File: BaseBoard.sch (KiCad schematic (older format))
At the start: 128 parts, among them U1 TLC5971PWP, U10 TLC5971PWP, U11 TLC5971PWP, U12 TLC5971PWP, U13 TLC5971PWP, U14 TLC5971PWP, U15 TLC5971PWP, U16 TLC5971PWP, U2 TLC5971PWP, U3 TLC5971PWP, U4 TLC5971PWP, U5 TLC5971PWP, U6 TLC5971PWP, U7 TLC5971PWP, U8 TLC5971PWP, U9 TLC5971PWP

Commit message: Reworked schematics
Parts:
- removed C1, C10, C11, C12, C13, C14, C15, C16, C17, C18, C19, C2, C20, C21, C22, C23, C24, C25, C26, C27, C28, C29, C3, C30, C31, C32, C4, C5, C6, C7, C8, C9: 1uF, symbol Device:C
- removed R1, R10, R11, R12, R13, R14, R15, R16, R2, R3, R4, R5, R6, R7, R8, R9: 1K, symbol Device:R
- removed U1, U10, U11, U12, U13, U14, U15, U16, U2, U3, U4, U5, U6, U7, U8, U9: TLC5971PWP, Package_SO:HTSSOP-20-1EP_4.4x6.5mm_P0.65mm_EP3.4x6.5mm_Mask2.75x3.43mm_ThermalVias, symbol Driver_LED:TLC5971PWP
- added ANOD1: Anodes, symbol BaseBoard:Anodes
- added C? (x32): 1uF, symbol Device:C
- added CNTL1: ESP32_NodeMCU, symbol BaseBoard:ESP32_NodeMCU
- added Q? (x8): IRLML6401TRPBF, digikey-footprints:SOT-23-3, symbol dk_Transistors-FETs-MOSFETs-Single:IRLML6401TRPBF
- added Q? (x8): MMBT2222A-7-F, digikey-footprints:SOT-23-3, symbol dk_Transistors-Bipolar-BJT-Single:MMBT2222A-7-F
- added R? (x32): 1K, symbol Device:R
- added R? (x8): 10, symbol Device:R
- added U1, U10, U11, U12, U13, U14, U15, U16, U2, U3, U4, U5, U6, U7, U8, U9: TLC59711PWPR, digikey-footprints:TSSOP-20-1EP_W4.4mm, symbol BaseBoard:TLC59711PWPR_Reordered
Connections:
- net labels added: VCC
- net labels removed: +5V
- wire segments 326 -> 463
- no-connect marks 0 -> 2

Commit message: Add anotations
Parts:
- removed C? (x32): 1uF, symbol Device:C
- removed R? (x16): 1K, symbol Device:R
- added C1, C10, C11, C12, C13, C14, C15, C16, C17, C18, C19, C2, C20, C21, C22, C23, C24, C25, C26, C27, C28, C29, C3, C30, C31, C32, C4, C5, C6, C7, C8, C9: 1uF, symbol Device:C
- added R25, R26, R27, R28, R29, R30, R31, R32, R33, R34, R35, R36, R37, R38, R39, R40: 1K, symbol Device:R
- gave numbers to parts that had none: 40

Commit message: Add footprints to common components
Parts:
- C1, C10, C11, C12, C13, C14, C15, C16, C17, C18, C19, C2, C20, C21, C22, C23, C24, C25, C26, C27, C28, C29, C3, C30, C31, C32, C4, C5, C6, C7, C8, C9: footprint (none) -> Capacitor_SMD:C_0805_2012Metric_Pad1.15x1.40mm_HandSolder
- CNTL1: footprint (none) -> BaseBoard:ESP32_NodeMCU
- R1, R10, R11, R12, R13, R14, R15, R16, R17, R18, R19, R2, R20, R21, R22, R23, R24, R25, R26, R27, R28, R29, R3, R30, R31, R32, R33, R34, R35, R36, R37, R38, R39, R4, R40, R5, R6, R7, R8, R9: footprint (none) -> Resistor_SMD:R_0805_2012Metric_Pad1.15x1.40mm_HandSolder

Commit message: Fix lots of fuckups
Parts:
- removed Q1, Q11, Q13, Q3, Q5, Q7, Q9: IRLML6401TRPBF, digikey-footprints:SOT-23-3, symbol dk_Transistors-FETs-MOSFETs-Single:IRLML6401TRPBF
- removed Q10, Q12, Q14, Q2, Q4, Q6, Q8: MMBT2222A-7-F, digikey-footprints:SOT-23-3, symbol dk_Transistors-Bipolar-BJT-Single:MMBT2222A-7-F
- removed U1, U10, U11, U12, U13, U14, U15, U16, U2, U3, U4, U5, U6, U7, U8, U9: TLC59711PWPR, digikey-footprints:TSSOP-20-1EP_W4.4mm, symbol BaseBoard:TLC59711PWPR_Reordered
- added Q1, Q11, Q13, Q3, Q5, Q7, Q9: MMBT2222A-7-F, digikey-footprints:SOT-23-3, symbol dk_Transistors-Bipolar-BJT-Single:MMBT2222A-7-F
- added Q10, Q12, Q14, Q2, Q4, Q6, Q8: IRLML6401TRPBF, digikey-footprints:SOT-23-3, symbol dk_Transistors-FETs-MOSFETs-Single:IRLML6401TRPBF
- added U1, U10, U11, U12, U13, U14, U15, U16, U2, U3, U4, U5, U6, U7, U8, U9: TLC5971PWPR, digikey-footprints:TSSOP-20-1EP_W4.4mm, symbol BaseBoard:TLC5971PWPR_Reordered
- R1, R10, R13, R16, R19, R22, R4, R7: footprint Resistor_SMD:R_0805_2012Metric_Pad1.15x1.40mm_HandSolder -> (none)
- R11, R14, R17, R2, R20, R23, R5, R8: value 10 -> 1K; footprint Resistor_SMD:R_0805_2012Metric_Pad1.15x1.40mm_HandSolder -> (none)
- R12, R15, R18, R21, R24, R3, R6, R9: value 1K -> 10; footprint Resistor_SMD:R_0805_2012Metric_Pad1.15x1.40mm_HandSolder -> (none)
- R25, R26, R27, R28, R29, R30, R31, R32, R33, R34, R35, R36, R37, R38, R39, R40: value 1K -> 3.3K
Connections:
- wire segments 463 -> 470
- no-connect marks 2 -> 28
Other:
- moved on the sheet: ANOD1, Q15, Q16

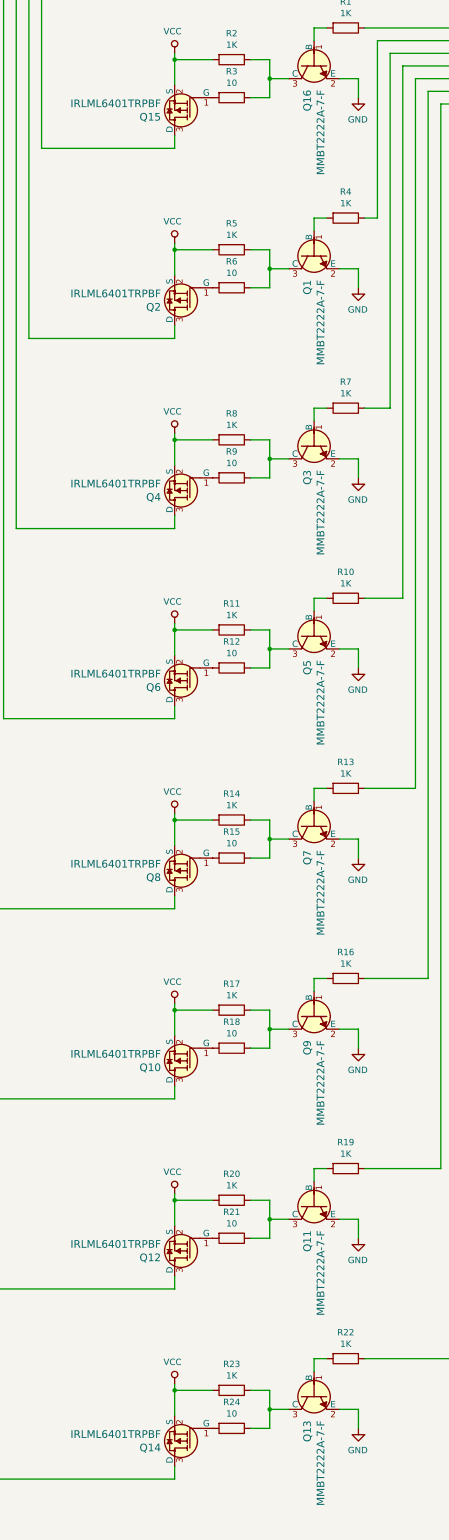
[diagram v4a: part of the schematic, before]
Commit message: Add PCB base
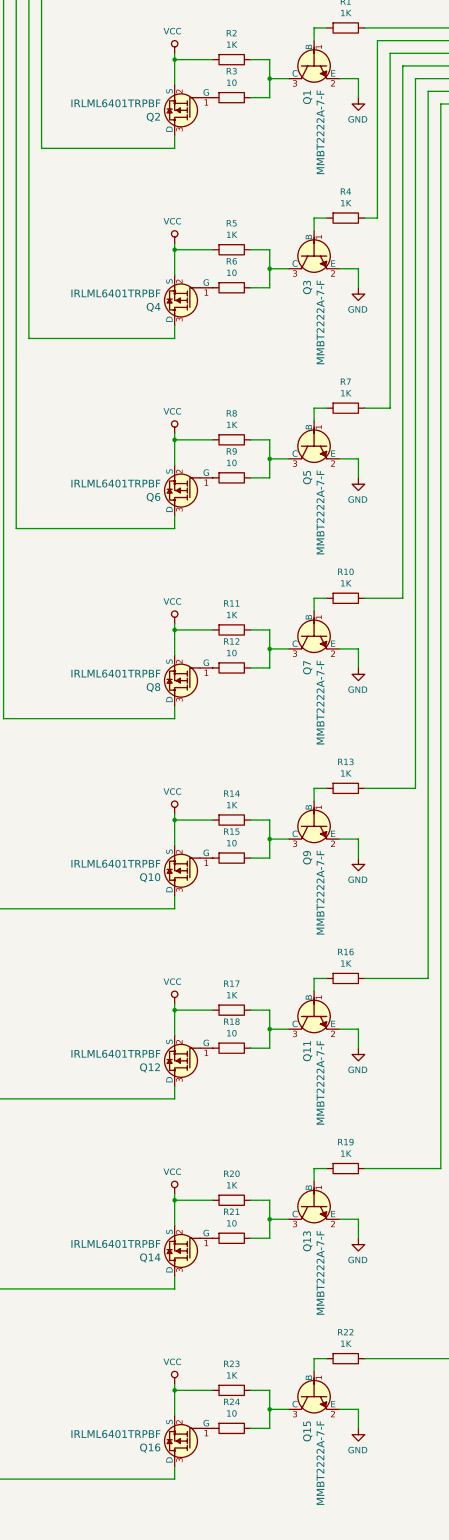
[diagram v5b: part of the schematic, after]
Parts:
- ANOD1: footprint (none) -> BaseBoard:Anodes
- R1, R10, R11, R12, R13, R14, R15, R16, R17, R18, R19, R2, R20, R21, R22, R23, R24, R3, R4, R5, R6, R7, R8, R9: footprint (none) -> Resistor_SMD:R_0805_2012Metric_Pad1.15x1.40mm_HandSolder
- renumbered Q16 to Q15, Q15 to Q16
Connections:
- net at R2.1, R3.1: now also Q1.3 (C); no longer Q15.3 (C)
- net at R3.2: now also Q2.1 (G); no longer Q16.1 (G)
- net at Q16.3 (D): now also ANOD1.8 (A8); no longer ANOD1.1 (A1)
- net at Q15.1 (B): now also R22.2; no longer R1.2
- net at Q1.1 (B): now also R1.2; no longer R4.2
- net at R5.1, R6.1: now also Q3.3 (C); no longer Q1.3 (C)
- net at R6.2: now also Q4.1 (G); no longer Q2.1 (G)
- net at Q2.3 (D): now also ANOD1.1 (A1); no longer ANOD1.2 (A2)
- net at Q3.1 (B): now also R4.2; no longer R7.2
- net at R8.1, R9.1: now also Q5.3 (C); no longer Q3.3 (C)
- net at R9.2: now also Q6.1 (G); no longer Q4.1 (G)
- net at Q4.3 (D): now also ANOD1.2 (A2); no longer ANOD1.3 (A3)
- net at Q5.1 (B): now also R7.2; no longer R10.2
- net at R11.1, R12.1: now also Q7.3 (C); no longer Q5.3 (C)
- net at R12.2: now also Q8.1 (G); no longer Q6.1 (G)
- net at Q6.3 (D): now also ANOD1.3 (A3); no longer ANOD1.4 (A4)
- net at Q7.1 (B): now also R10.2; no longer R13.2
- net at R14.1, R15.1: now also Q9.3 (C); no longer Q7.3 (C)
- net at R15.2: now also Q10.1 (G); no longer Q8.1 (G)
- net at Q8.3 (D): now also ANOD1.4 (A4); no longer ANOD1.5 (A5)
- net at Q9.1 (B): now also R13.2; no longer R16.2
- net at R17.1, R18.1: now also Q11.3 (C); no longer Q9.3 (C)
- net at R18.2: now also Q12.1 (G); no longer Q10.1 (G)
- net at Q10.3 (D): now also ANOD1.5 (A5); no longer ANOD1.6 (A6)
- net at Q11.1 (B): now also R16.2; no longer R19.2
- net at R20.1, R21.1: now also Q13.3 (C); no longer Q11.3 (C)
- net at R21.2: now also Q14.1 (G); no longer Q12.1 (G)
- net at Q12.3 (D): now also ANOD1.6 (A6); no longer ANOD1.7 (A7)
- net at Q13.1 (B): now also R19.2; no longer R22.2
- net at R23.1, R24.1: now also Q15.3 (C); no longer Q13.3 (C)
- net at R24.2: now also Q16.1 (G); no longer Q14.1 (G)
- net at Q14.3 (D): now also ANOD1.7 (A7); no longer ANOD1.8 (A8)
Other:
- moved on the sheet: Q1, Q10, Q11, Q12, Q13, Q14, Q15, Q16, Q2, Q3, Q4, Q5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

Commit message: Update footprints
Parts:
- U1, U10, U11, U12, U13, U14, U15, U16, U2, U3, U4, U5, U6, U7, U8, U9: footprint digikey-footprints:TSSOP-20-1EP_W4.4mm -> Package_SO:HTSSOP-20-1EP_4.4x6.5mm_P0.65mm_EP3.4x6.5mm_Mask2.75x3.43mm_ThermalVias
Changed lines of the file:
@@
 F 0 "U4" H 18150 3453 60  0000 C CNN
 F 1 "TLC5971PWPR" H 18150 3347 60  0000 C CNN
-F 2 "digikey-footprints:TSSOP-20-1EP_W4.4mm" H 18300 2950 60  0001 L CNN
+F 2 "Package_SO:HTSSOP-20-1EP_4.4x6.5mm_P0.65mm_EP3.4x6.5mm_Mask2.75x3.43mm_ThermalVias" H 18300 2950 60  0001 L CNN
 F 3 "http://www.ti.com/general/docs/suppproductinfo.tsp?distId=10&gotoUrl=http%3A%2F%2Fwww.ti.com%2Flit%2Fgpn%2Ftlc5971" H 18300 3050 60  0001 L CNN
 F 4 "296-27796-1-ND" H 18300 3150 60  0001 L CNN "Digi-Key_PN"
@@
 F 0 "U3" H 15900 3453 60  0000 C CNN
 F 1 "TLC5971PWPR" H 15900 3347 60  0000 C CNN
-F 2 "digikey-footprints:TSSOP-20-1EP_W4.4mm" H 16050 2950 60  0001 L CNN
+F 2 "Package_SO:HTSSOP-20-1EP_4.4x6.5mm_P0.65mm_EP3.4x6.5mm_Mask2.75x3.43mm_ThermalVias" H 16050 2950 60  0001 L CNN
 F 3 "http://www.ti.com/general/docs/suppproductinfo.tsp?distId=10&gotoUrl=http%3A%2F%2Fwww.ti.com%2Flit%2Fgpn%2Ftlc5971" H 16050 3050 60  0001 L CNN
 F 4 "296-27796-1-ND" H 16050 3150 60  0001 L CNN "Digi-Key_PN"
@@
 F 0 "U2" H 13650 3403 60  0000 C CNN
 F 1 "TLC5971PWPR" H 13650 3297 60  0000 C CNN
-F 2 "digikey-footprints:TSSOP-20-1EP_W4.4mm" H 13800 2900 60  0001 L CNN
+F 2 "Package_SO:HTSSOP-20-1EP_4.4x6.5mm_P0.65mm_EP3.4x6.5mm_Mask2.75x3.43mm_ThermalVias" H 13800 2900 60  0001 L CNN
 F 3 "http://www.ti.com/general/docs/suppproductinfo.tsp?distId=10&gotoUrl=http%3A%2F%2Fwww.ti.com%2Flit%2Fgpn%2Ftlc5971" H 13800 3000 60  0001 L CNN
 F 4 "296-27796-1-ND" H 13800 3100 60  0001 L CNN "Digi-Key_PN"
@@
 F 0 "U1" H 11400 3403 60  0000 C CNN
 F 1 "TLC5971PWPR" H 11400 3297 60  0000 C CNN
-F 2 "digikey-footprints:TSSOP-20-1EP_W4.4mm" H 11550 2900 60  0001 L CNN
+F 2 "Package_SO:HTSSOP-20-1EP_4.4x6.5mm_P0.65mm_EP3.4x6.5mm_Mask2.75x3.43mm_ThermalVias" H 11550 2900 60  0001 L CNN
 F 3 "http://www.ti.com/general/docs/suppproductinfo.tsp?distId=10&gotoUrl=http%3A%2F%2Fwww.ti.com%2Flit%2Fgpn%2Ftlc5971" H 11550 3000 60  0001 L CNN
 F 4 "296-27796-1-ND" H 11550 3100 60  0001 L CNN "Digi-Key_PN"
@@
 F 0 "U8" H 18150 6553 60  0000 C CNN
 F 1 "TLC5971PWPR" H 18150 6447 60  0000 C CNN
-F 2 "digikey-footprints:TSSOP-20-1EP_W4.4mm" H 18300 6050 60  0001 L CNN
+F 2 "Package_SO:HTSSOP-20-1EP_4.4x6.5mm_P0.65mm_EP3.4x6.5mm_Mask2.75x3.43mm_ThermalVias" H 18300 6050 60  0001 L CNN
 F 3 "http://www.ti.com/general/docs/suppproductinfo.tsp?distId=10&gotoUrl=http%3A%2F%2Fwww.ti.com%2Flit%2Fgpn%2Ftlc5971" H 18300 6150 60  0001 L CNN
 F 4 "296-27796-1-ND" H 18300 6250 60  0001 L CNN "Digi-Key_PN"
@@
 F 0 "U7" H 15900 6553 60  0000 C CNN
 F 1 "TLC5971PWPR" H 15900 6447 60  0000 C CNN
-F 2 "digikey-footprints:TSSOP-20-1EP_W4.4mm" H 16050 6050 60  0001 L CNN
+F 2 "Package_SO:HTSSOP-20-1EP_4.4x6.5mm_P0.65mm_EP3.4x6.5mm_Mask2.75x3.43mm_ThermalVias" H 16050 6050 60  0001 L CNN
 F 3 "http://www.ti.com/general/docs/suppproductinfo.tsp?distId=10&gotoUrl=http%3A%2F%2Fwww.ti.com%2Flit%2Fgpn%2Ftlc5971" H 16050 6150 60  0001 L CNN
 F 4 "296-27796-1-ND" H 16050 6250 60  0001 L CNN "Digi-Key_PN"
@@
 F 0 "U6" H 13650 6503 60  0000 C CNN
 F 1 "TLC5971PWPR" H 13650 6397 60  0000 C CNN
-F 2 "digikey-footprints:TSSOP-20-1EP_W4.4mm" H 13800 6000 60  0001 L CNN
+F 2 "Package_SO:HTSSOP-20-1EP_4.4x6.5mm_P0.65mm_EP3.4x6.5mm_Mask2.75x3.43mm_ThermalVias" H 13800 6000 60  0001 L CNN
 F 3 "http://www.ti.com/general/docs/suppproductinfo.tsp?distId=10&gotoUrl=http%3A%2F%2Fwww.ti.com%2Flit%2Fgpn%2Ftlc5971" H 13800 6100 60  0001 L CNN
 F 4 "296-27796-1-ND" H 13800 6200 60  0001 L CNN "Digi-Key_PN"
@@
 F 0 "U5" H 11400 6503 60  0000 C CNN
 F 1 "TLC5971PWPR" H 11400 6397 60  0000 C CNN
-F 2 "digikey-footprints:TSSOP-20-1EP_W4.4mm" H 11550 6000 60  0001 L CNN
+F 2 "Package_SO:HTSSOP-20-1EP_4.4x6.5mm_P0.65mm_EP3.4x6.5mm_Mask2.75x3.43mm_ThermalVias" H 11550 6000 60  0001 L CNN
 F 3 "http://www.ti.com/general/docs/suppproductinfo.tsp?distId=10&gotoUrl=http%3A%2F%2Fwww.ti.com%2Flit%2Fgpn%2Ftlc5971" H 11550 6100 60  0001 L CNN
 F 4 "296-27796-1-ND" H 11550 6200 60  0001 L CNN "Digi-Key_PN"
@@
 F 0 "U12" H 18150 9653 60  0000 C CNN
 F 1 "TLC5971PWPR" H 18150 9547 60  0000 C CNN
-F 2 "digikey-footprints:TSSOP-20-1EP_W4.4mm" H 18300 9150 60  0001 L CNN
+F 2 "Package_SO:HTSSOP-20-1EP_4.4x6.5mm_P0.65mm_EP3.4x6.5mm_Mask2.75x3.43mm_ThermalVias" H 18300 9150 60  0001 L CNN
 F 3 "http://www.ti.com/general/docs/suppproductinfo.tsp?distId=10&gotoUrl=http%3A%2F%2Fwww.ti.com%2Flit%2Fgpn%2Ftlc5971" H 18300 9250 60  0001 L CNN
 F 4 "296-27796-1-ND" H 18300 9350 60  0001 L CNN "Digi-Key_PN"
@@
 F 0 "U11" H 15900 9653 60  0000 C CNN
 F 1 "TLC5971PWPR" H 15900 9547 60  0000 C CNN
-F 2 "digikey-footprints:TSSOP-20-1EP_W4.4mm" H 16050 9150 60  0001 L CNN
+F 2 "Package_SO:HTSSOP-20-1EP_4.4x6.5mm_P0.65mm_EP3.4x6.5mm_Mask2.75x3.43mm_ThermalVias" H 16050 9150 60  0001 L CNN
 F 3 "http://www.ti.com/general/docs/suppproductinfo.tsp?distId=10&gotoUrl=http%3A%2F%2Fwww.ti.com%2Flit%2Fgpn%2Ftlc5971" H 16050 9250 60  0001 L CNN
 F 4 "296-27796-1-ND" H 16050 9350 60  0001 L CNN "Digi-Key_PN"
@@
 F 0 "U10" H 13650 9603 60  0000 C CNN
 F 1 "TLC5971PWPR" H 13650 9497 60  0000 C CNN
-F 2 "digikey-footprints:TSSOP-20-1EP_W4.4mm" H 13800 9100 60  0001 L CNN
+F 2 "Package_SO:HTSSOP-20-1EP_4.4x6.5mm_P0.65mm_EP3.4x6.5mm_Mask2.75x3.43mm_ThermalVias" H 13800 9100 60  0001 L CNN
 F 3 "http://www.ti.com/general/docs/suppproductinfo.tsp?distId=10&gotoUrl=http%3A%2F%2Fwww.ti.com%2Flit%2Fgpn%2Ftlc5971" H 13800 9200 60  0001 L CNN
 F 4 "296-27796-1-ND" H 13800 9300 60  0001 L CNN "Digi-Key_PN"
@@
 F 0 "U9" H 11400 9603 60  0000 C CNN
 F 1 "TLC5971PWPR" H 11400 9497 60  0000 C CNN
-F 2 "digikey-footprints:TSSOP-20-1EP_W4.4mm" H 11550 9100 60  0001 L CNN
+F 2 "Package_SO:HTSSOP-20-1EP_4.4x6.5mm_P0.65mm_EP3.4x6.5mm_Mask2.75x3.43mm_ThermalVias" H 11550 9100 60  0001 L CNN
 F 3 "http://www.ti.com/general/docs/suppproductinfo.tsp?distId=10&gotoUrl=http%3A%2F%2Fwww.ti.com%2Flit%2Fgpn%2Ftlc5971" H 11550 9200 60  0001 L CNN
 F 4 "296-27796-1-ND" H 11550 9300 60  0001 L CNN "Digi-Key_PN"
@@
 F 0 "U16" H 18150 12753 60  0000 C CNN
 F 1 "TLC5971PWPR" H 18150 12647 60  0000 C CNN
-F 2 "digikey-footprints:TSSOP-20-1EP_W4.4mm" H 18300 12250 60  0001 L CNN
+F 2 "Package_SO:HTSSOP-20-1EP_4.4x6.5mm_P0.65mm_EP3.4x6.5mm_Mask2.75x3.43mm_ThermalVias" H 18300 12250 60  0001 L CNN
 F 3 "http://www.ti.com/general/docs/suppproductinfo.tsp?distId=10&gotoUrl=http%3A%2F%2Fwww.ti.com%2Flit%2Fgpn%2Ftlc5971" H 18300 12350 60  0001 L CNN
 F 4 "296-27796-1-ND" H 18300 12450 60  0001 L CNN "Digi-Key_PN"
@@
 F 0 "U15" H 15900 12753 60  0000 C CNN
 F 1 "TLC5971PWPR" H 15900 12647 60  0000 C CNN
-F 2 "digikey-footprints:TSSOP-20-1EP_W4.4mm" H 16050 12250 60  0001 L CNN
+F 2 "Package_SO:HTSSOP-20-1EP_4.4x6.5mm_P0.65mm_EP3.4x6.5mm_Mask2.75x3.43mm_ThermalVias" H 16050 12250 60  0001 L CNN
 F 3 "http://www.ti.com/general/docs/suppproductinfo.tsp?distId=10&gotoUrl=http%3A%2F%2Fwww.ti.com%2Flit%2Fgpn%2Ftlc5971" H 16050 12350 60  0001 L CNN
 F 4 "296-27796-1-ND" H 16050 12450 60  0001 L CNN "Digi-Key_PN"
@@
 F 0 "U14" H 13650 12703 60  0000 C CNN
 F 1 "TLC5971PWPR" H 13650 12597 60  0000 C CNN
-F 2 "digikey-footprints:TSSOP-20-1EP_W4.4mm" H 13800 12200 60  0001 L CNN
+F 2 "Package_SO:HTSSOP-20-1EP_4.4x6.5mm_P0.65mm_EP3.4x6.5mm_Mask2.75x3.43mm_ThermalVias" H 13800 12200 60  0001 L CNN
 F 3 "http://www.ti.com/general/docs/suppproductinfo.tsp?distId=10&gotoUrl=http%3A%2F%2Fwww.ti.com%2Flit%2Fgpn%2Ftlc5971" H 13800 12300 60  0001 L CNN
 F 4 "296-27796-1-ND" H 13800 12400 60  0001 L CNN "Digi-Key_PN"
@@
 F 0 "U13" H 11400 12703 60  0000 C CNN
 F 1 "TLC5971PWPR" H 11400 12597 60  0000 C CNN
-F 2 "digikey-footprints:TSSOP-20-1EP_W4.4mm" H 11550 12200 60  0001 L CNN
+F 2 "Package_SO:HTSSOP-20-1EP_4.4x6.5mm_P0.65mm_EP3.4x6.5mm_Mask2.75x3.43mm_ThermalVias" H 11550 12200 60  0001 L CNN
 F 3 "http://www.ti.com/general/docs/suppproductinfo.tsp?distId=10&gotoUrl=http%3A%2F%2Fwww.ti.com%2Flit%2Fgpn%2Ftlc5971" H 11550 12300 60  0001 L CNN
 F 4 "296-27796-1-ND" H 11550 12400 60  0001 L CNN "Digi-Key_PN"
